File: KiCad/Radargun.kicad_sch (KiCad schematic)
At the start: 6 parts, among them J1 Li-Po batterij, J2 USB_C_Receptacle, U1 ESP32-S3-WROOM-1, U2 TP4056

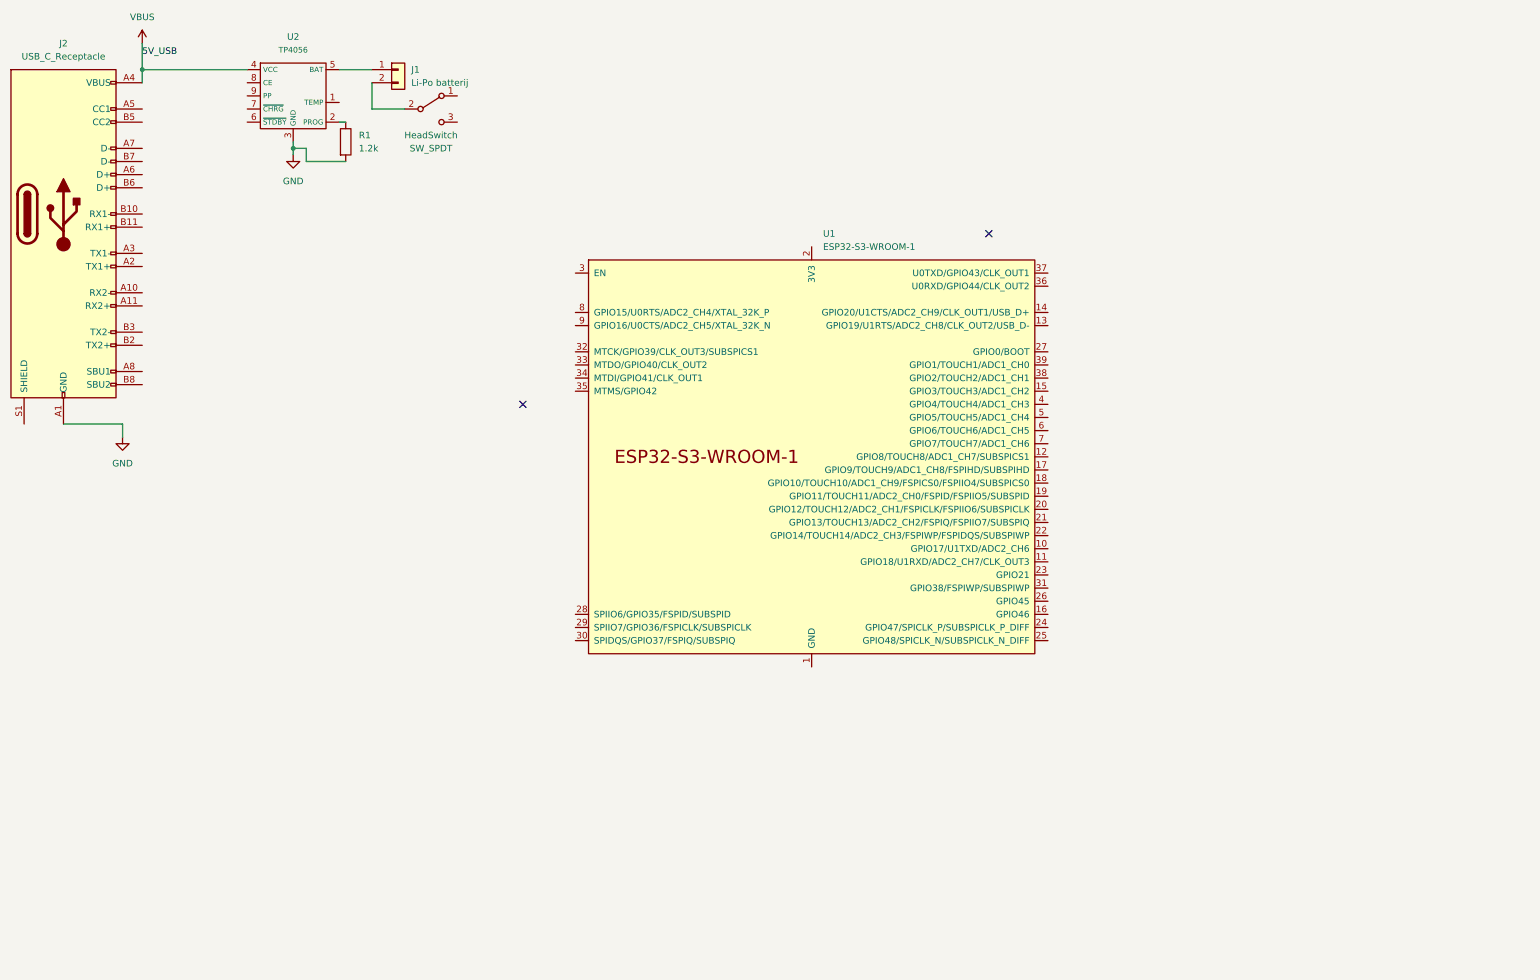
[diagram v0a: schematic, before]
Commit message: Complete Phase 1 Schematic Capture (No ERC errors)
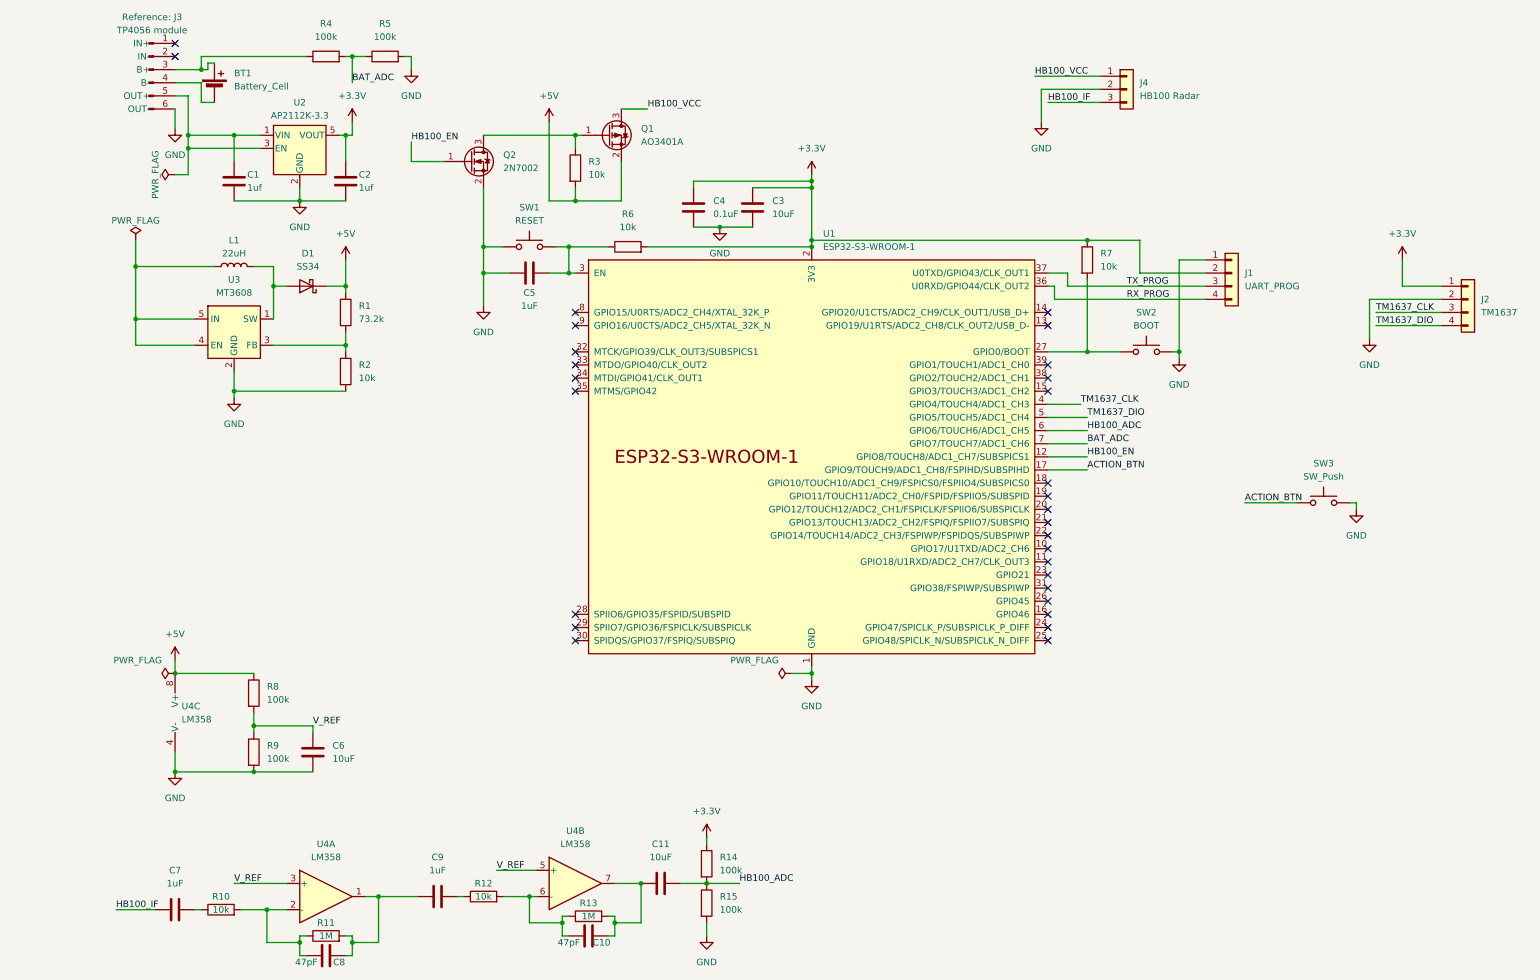
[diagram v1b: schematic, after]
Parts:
- removed HeadSwitch: SW_SPDT, symbol Switch:SW_SPDT
- removed J1: Li-Po batterij, symbol Connector_Generic:Conn_01x02
- removed J2: USB_C_Receptacle, symbol Connector:USB_C_Receptacle
- removed U2: TP4056, Package_SO:SOIC-8-1EP_3.9x4.9mm_P1.27mm_EP2.29x3mm, symbol tp4056:TP4056
- added BT1: Battery_Cell, symbol Device:Battery_Cell
- added C1, C2: 1uf, symbol Device:C
- added C10, C8: 47pF, symbol Device:C
- added C11, C3, C6: 10uF, symbol Device:C
- added C4: 0.1uF, symbol Device:C
- added C5, C7, C9: 1uF, symbol Device:C
- added D1: SS34, symbol Device:D_Schottky
- added J1: UART_PROG, symbol Connector_Generic:Conn_01x04
- added J2: TM1637, symbol Connector_Generic:Conn_01x04
- added J3: TP4056 module, symbol Connector:Conn_01x06_Pin
- added J4: HB100 Radar, symbol Connector_Generic:Conn_01x03
- added L1: 22uH, symbol Device:L
- added Q1: AO3401A, Package_TO_SOT_SMD:SOT-23, symbol Transistor_FET:AO3401A
- added Q2: 2N7002, Package_TO_SOT_SMD:SOT-23, symbol Transistor_FET:2N7002
- added R10, R12, R2, R3, R6, R7: 10k, symbol Device:R
- added R11, R13: 1M, symbol Device:R
- added R14, R15, R4, R5, R8, R9: 100k, symbol Device:R
- added SW1: RESET, symbol Switch:SW_Push
- added SW2: BOOT, symbol Switch:SW_Push
- added SW3: SW_Push, symbol Switch:SW_Push
- added U2: AP2112K-3.3, Package_TO_SOT_SMD:SOT-23-5, symbol Regulator_Linear:AP2112K-3.3
- added U3: MT3608, Package_TO_SOT_SMD:SOT-23-6, symbol Regulator_Switching:MT3608
- added U4: LM358, symbol Amplifier_Operational:LM358
- R1: value 1.2k -> 73.2k
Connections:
- net GND: now also U1.1 (GND), U1.40 (GND), U1.41 (GND), C1.2, C2.2, C3.2, C4.2, C5.1, C6.2, J1.1 (Pin_1), J2.2 (Pin_2), J3.6 (OUT-), J4.2 (Pin_2), Q2.2 (S), R15.2, R2.2, R5.2, R9.2, SW1.1, SW2.2, SW3.2, U2.2 (GND), U3.2 (GND), U4.4 (V-); no longer R1.2
- net HB100_EN: now reaches U1.12 (GPIO8/TOUCH8/ADC1_CH7/SUBSPICS1)
- net HB100_EN: now also Q2.1 (G)
- net ACTION_BTN: now reaches U1.17 (GPIO9/TOUCH9/ADC1_CH8/FSPIHD/SUBSPIHD)
- net ACTION_BTN: now also SW3.1
- net +3.3V: now reaches U1.2 (3V3)
- net +3.3V: now also C2.1, C3.1, C4.1, J1.2 (Pin_2), J2.1 (Pin_1), R14.1, R6.2, R7.1, U2.5 (VOUT)
- net at U1.27 (GPIO0/BOOT): now also R7.2, SW2.1
- net at U1.3 (EN): now also C5.2, R6.1, SW1.2
- net RX_PROG : now reaches U1.36 (U0RXD/GPIO44/CLK_OUT2)
- net RX_PROG : now also J1.4 (Pin_4)
- net TX_PROG : now reaches U1.37 (U0TXD/GPIO43/CLK_OUT1)
- net TX_PROG : now also J1.3 (Pin_3)
- net TM1637_CLK : now reaches U1.4 (GPIO4/TOUCH4/ADC1_CH3)
- net TM1637_CLK : now also J2.3 (Pin_3)
- net TM1637_DIO: now reaches U1.5 (GPIO5/TOUCH5/ADC1_CH4)
- net TM1637_DIO: now also J2.4 (Pin_4)
- net HB100_ADC : now reaches U1.6 (GPIO6/TOUCH6/ADC1_CH5)
- net HB100_ADC : now also C11.2, R14.2, R15.1
- net BAT_ADC: now reaches U1.7 (GPIO7/TOUCH7/ADC1_CH6)
- net BAT_ADC: now also R4.2, R5.1
- net +5V: now reaches R1.1
- net +5V: now also D1.1 (K), Q1.2 (S), R3.2, R8.1, U4.8 (V+)
- new net: C10.2, C11.1, R13.2, U4.7
- new net: R1.2, R2.1, U3.3 (FB)
- new net: Q1.1 (G), Q2.3 (D), R3.1
- new net: C8.1, R10.2, R11.1, U4.2 (-)
- new net: C8.2, C9.1, R11.2, U4.1
- new net: C10.1, R12.2, R13.1, U4.6 (-)
- new net: C1.1, J3.5 (OUT+), U2.1 (VIN), U2.3 (EN)
- new net: C7.2, R10.1
- new net: C9.2, R12.1
- new net: BT1.1 (+), J3.3 (B+), R4.1
- new net: D1.2 (A), L1.2, U3.1 (SW)
- new net: L1.1, U3.4 (EN), U3.5 (IN)
- new net: BT1.2 (-), J3.4 (B-)
- new net HB100_IF: C7.1, J4.3 (Pin_3)
- new net HB100_VCC: J4.1 (Pin_1), Q1.3 (D)
- new net V_REF: C6.1, R8.2, R9.1, U4.3 (+), U4.5 (+)
- no-connect marks 2 -> 29

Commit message: Add safety net components to KiCad schematic
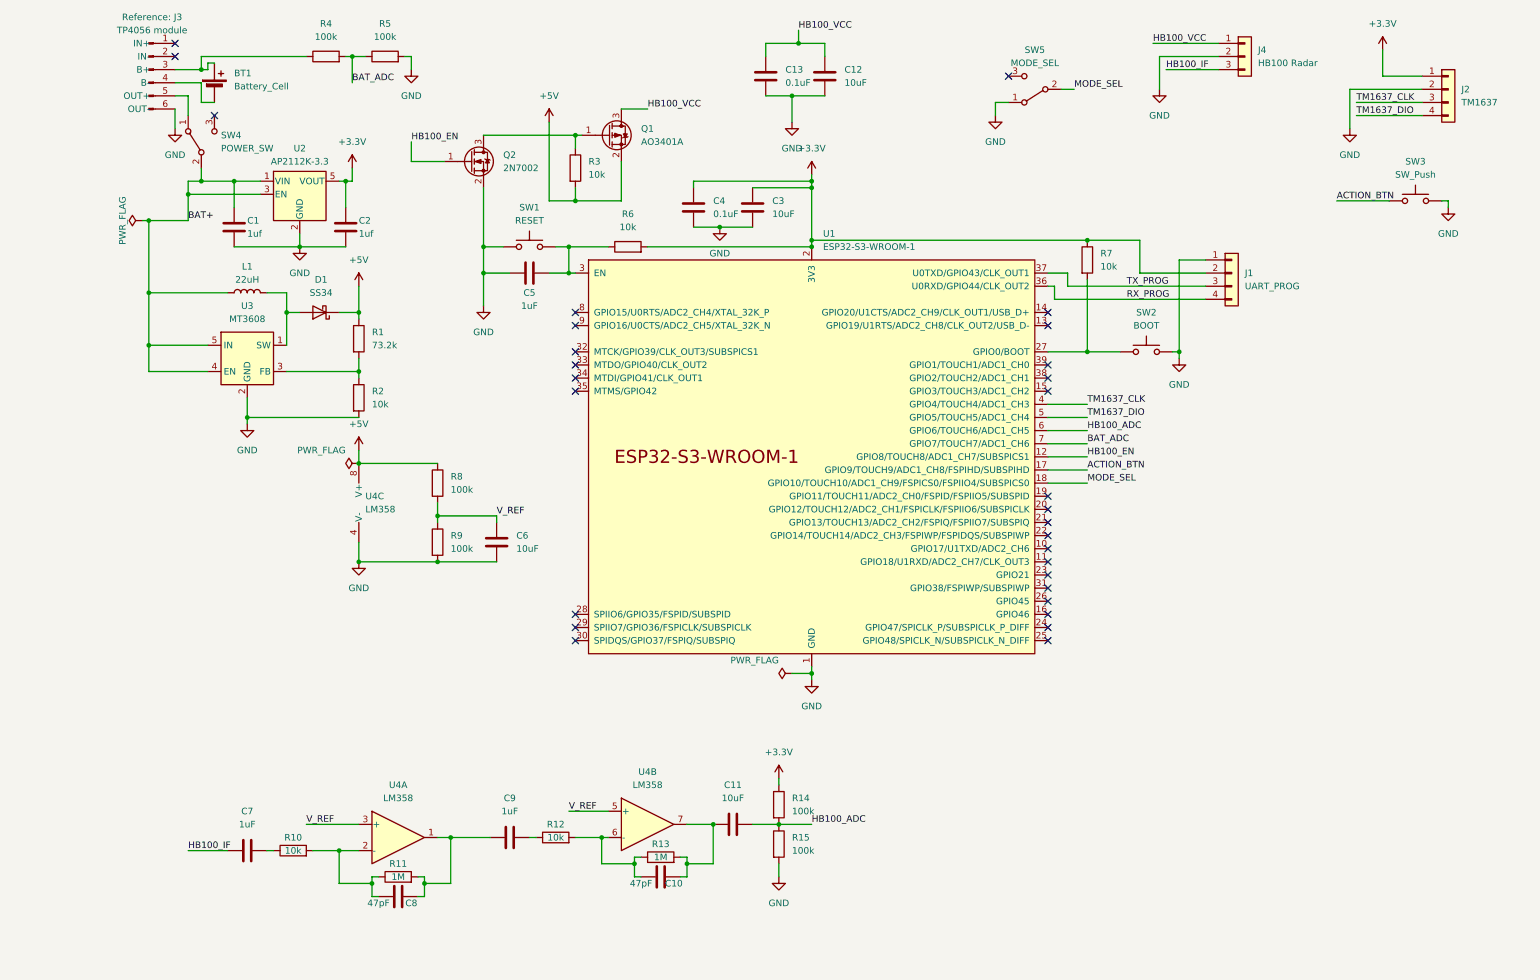
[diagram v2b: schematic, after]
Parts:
- added C12: 10uF, symbol Device:C
- added C13: 0.1uF, symbol Device:C
- added SW4: POWER_SW, symbol Switch:SW_SPDT
- added SW5: MODE_SEL, symbol Switch:SW_SPDT
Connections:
- net GND: now also C12.2, C13.2, SW5.1 (A)
- net HB100_VCC: now also C12.1, C13.1
- net MODE_SEL: now reaches U1.18 (GPIO10/TOUCH10/ADC1_CH9/FSPICS0/FSPIIO4/SUBSPICS0)
- net MODE_SEL: now also SW5.2 (B)
- net BAT+: now reaches C1.1, U2.1 (VIN), U2.3 (EN)
- net BAT+: now also L1.1, U3.4 (EN), U3.5 (IN), SW4.2 (B); no longer J3.5 (OUT+)
- new net: J3.5 (OUT+), SW4.1 (A)
- no-connect marks 29 -> 30
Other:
- moved on the sheet: C1, C10, C11, C2, C6, C7, C8, C9, D1, J2, J4, L1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

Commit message: Start design PCB Layout
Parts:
- added D2: PWR_LED, LED_SMD:LED_0805_2012Metric_Pad1.15x1.40mm_HandSolder, symbol Device:LED
- added D3: STATUS_LED, LED_SMD:LED_0805_2012Metric_Pad1.15x1.40mm_HandSolder, symbol Device:LED
- added H1, H2, H3, H4: MountingHole, MountingHole:MountingHole_3.2mm_M3, symbol Mechanical:MountingHole
- added R16: 470, Resistor_SMD:R_0805_2012Metric_Pad1.20x1.40mm_HandSolder, symbol Device:R
- added R17: 220, Resistor_SMD:R_0805_2012Metric_Pad1.20x1.40mm_HandSolder, symbol Device:R
- added R18, R19: 10k, Resistor_SMD:R_0805_2012Metric_Pad1.20x1.40mm_HandSolder, symbol Device:R
- BT1: footprint (none) -> Connector_JST:JST_PH_B2B-PH-K_1x02_P2.00mm_Vertical
- C1, C10, C11, C12, C13, C2, C3, C4, C5, C6, C7, C8, C9: footprint (none) -> Capacitor_SMD:C_0805_2012Metric_Pad1.18x1.45mm_HandSolder
- D1: footprint (none) -> Diode_SMD:D_SMA
- J1, J2: footprint (none) -> Connector_PinHeader_2.54mm:PinHeader_1x04_P2.54mm_Vertical
- J3: footprint (none) -> Connector_PinHeader_2.54mm:PinHeader_1x06_P2.54mm_Vertical
- J4: footprint (none) -> Connector_PinHeader_2.54mm:PinHeader_1x03_P2.54mm_Vertical
- L1: footprint (none) -> Inductor_SMD:L_1210_3225Metric_Pad1.42x2.65mm_HandSolder
- R1, R10, R11, R12, R13, R14, R15, R2, R3, R4, R5, R6, R7, R8, R9: footprint (none) -> Resistor_SMD:R_0805_2012Metric_Pad1.20x1.40mm_HandSolder
- SW1, SW2, SW3: footprint (none) -> Button_Switch_THT:SW_PUSH_6mm
- SW4, SW5: footprint (none) -> Button_Switch_THT:SW_Slide_SPDT_SS12D00
- U4: footprint (none) -> Package_SO:SOIC-8_3.9x4.9mm_P1.27mm
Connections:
- net +3.3V: now also D2.2 (A), R18.2, R19.2
- net ACTION_BTN: now also R18.1
- net GND: now also D3.1 (K), R16.2
- net MODE_SEL: now also R19.1
- net at U1.16 (GPIO46): now also R17.1
- new net: D3.2 (A), R17.2
- new net: D2.1 (K), R16.1
- no-connect marks 30 -> 29
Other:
- moved on the sheet: SW3

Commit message: PCB layout guide added
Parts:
- SW4, SW5: footprint Button_Switch_THT:SW_Slide_SPDT_SS12D00 -> Library:SS12D00
- U1: footprint PCM_Espressif:ESP32-S3-WROOM-1 -> Library:ESP32-S3-WROOM-1
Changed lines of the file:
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@@
       (effects (font (size 1.27 1.27)) (justify left))
     )
-    (property "Footprint" "PCM_Espressif:ESP32-S3-WROOM-1" (at 149.86 147.32 0)
+    (property "Footprint" "Library:ESP32-S3-WROOM-1" (at 149.86 147.32 0)
       (effects (font (size 1.27 1.27)) hide)
     )
@@
       (effects (font (size 1.27 1.27)) (justify right))
     )
-    (property "Footprint" "Button_Switch_THT:SW_Slide_SPDT_SS12D00" (at 29.21 38.1 0)
+    (property "Footprint" "Library:SS12D00" (at 29.21 38.1 0)
       (effects (font (size 1.27 1.27)) hide)
     )
@@
       (effects (font (size 1.27 1.27)))
     )
-    (property "Footprint" "Button_Switch_THT:SW_Slide_SPDT_SS12D00" (at 190.5 27.94 0)
-      (effects (font (size 1.27 1.27)) hide)
-    )
+    (property "Footprint" "Library:SS12D00" (at 190.5 27.94 0)
+      (effects (font (size 1.27 1.27)) hide)
+    )
